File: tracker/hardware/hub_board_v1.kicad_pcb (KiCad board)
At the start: 2 copper layers, 50 x 40 mm, 28 parts, among them U1 RP2040-Zero, U2 LoRa2021, U3 MAX-M10S, U4 MS5611, U5 TPS7A02

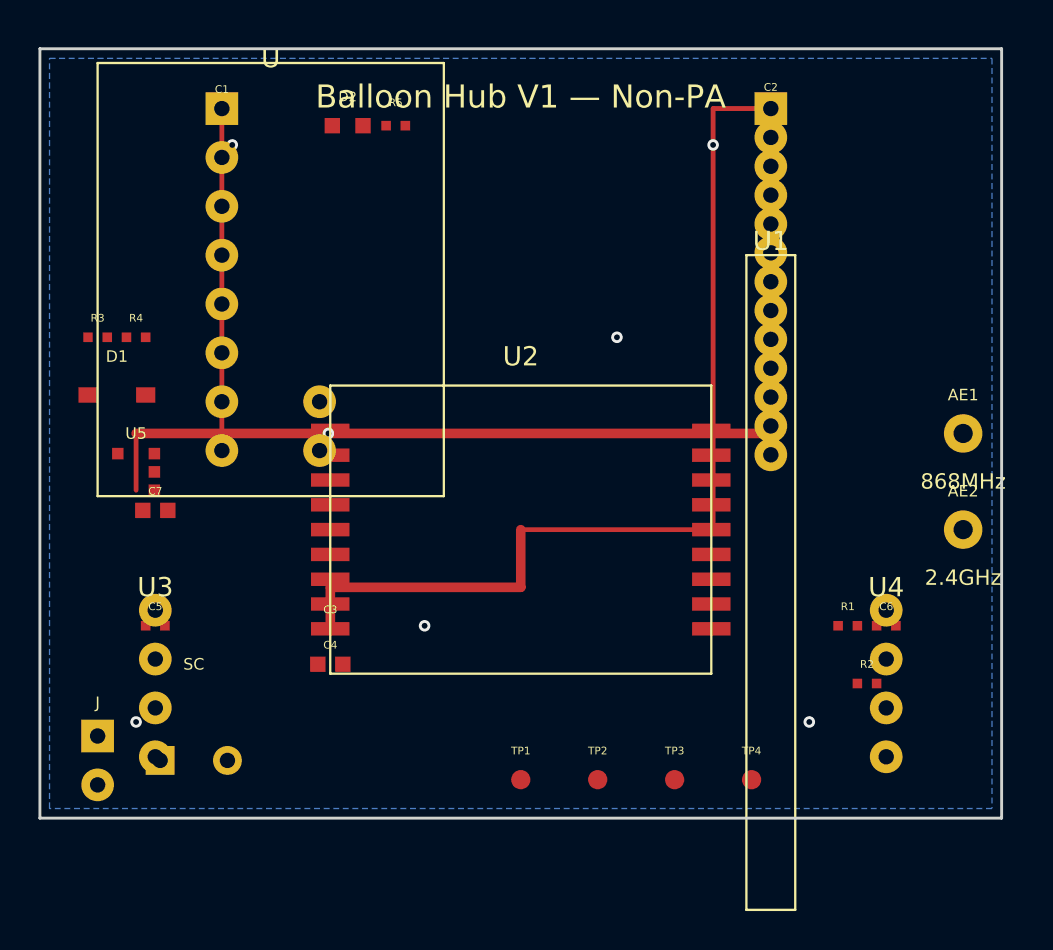
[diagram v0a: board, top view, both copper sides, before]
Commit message: feat(pcb): V1 all signal nets routed — 84 traces, SPI/UART/I2C/RF
84 traces: power (3V3, VCAP, SOLAR), SPI (SCK/MOSI/MISO/NSS),
control (BUSY/IRQ/RST), UART (ESP<->RP, GPS), I2C (SDA/SCL),
RF antenna (sub-868 + 2.4G), status LED, voltage divider.
B.Cu used for crossing signals. 7 GND stitching vias.

46 unconnected: decoupling caps + pull-ups needing local traces.
311 violations: clearance (tracks near pads) — fixable in KiCad GUI.
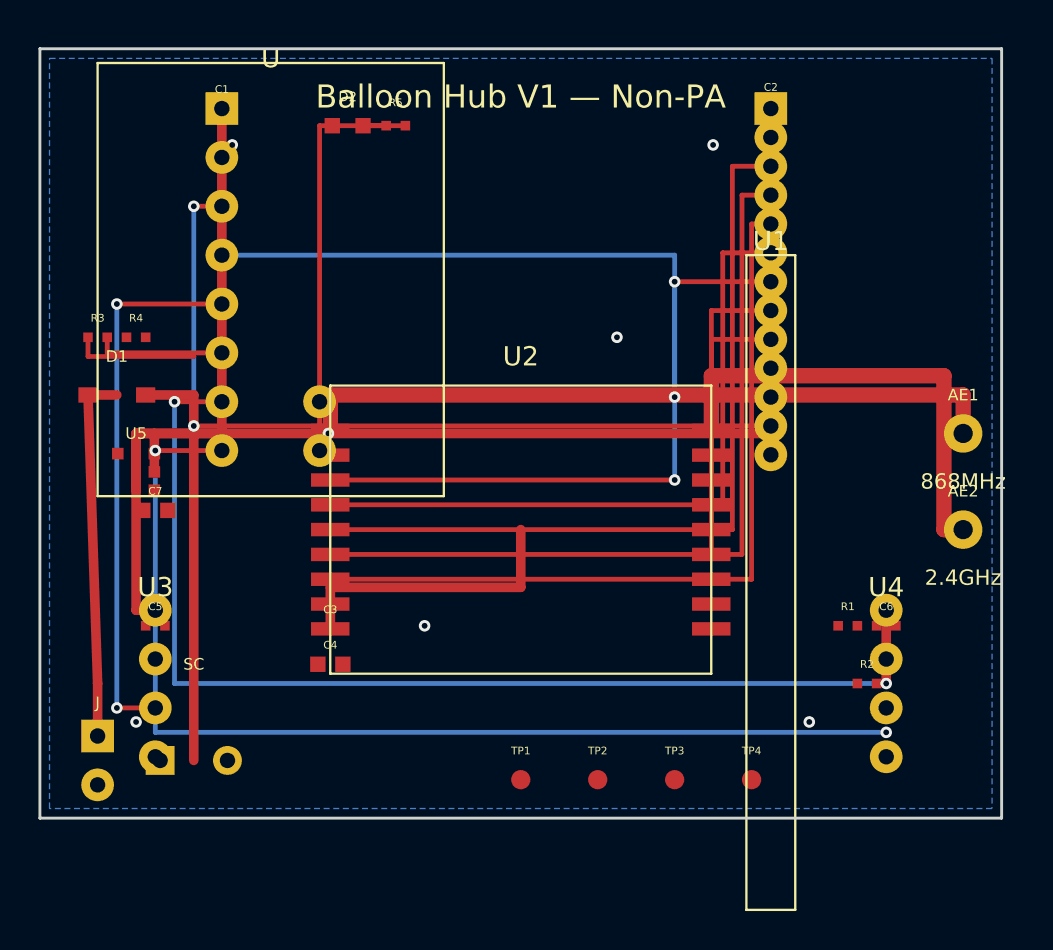
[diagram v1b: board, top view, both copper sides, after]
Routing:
- net I2C_SCL: track 0.00 -> 56.1 mm, vias 0 -> 2
- net I2C_SDA: track 0.00 -> 54.1 mm, vias 0 -> 2
- net ESP_TX_RP2040_RX: track 0.00 -> 42.9 mm, vias 0 -> 2
- net SPI0_MOSI: track 0.00 -> 41.6 mm
- net SPI0_MISO: track 0.00 -> 41.4 mm
- net RF_SUB_868: track 0.00 -> 36.7 mm
- net SPI0_NSS: track 0.00 -> 36.0 mm
- net RP2040_TX_ESP_RX: track 0.00 -> 35.9 mm, vias 0 -> 2
- net LR2021_BUSY: track 0.00 -> 33.2 mm, vias 0 -> 2
- net VCAP: track 0.00 -> 30.0 mm
- net GPS_TX_ESP_RX: track 0.00 -> 28.5 mm, vias 0 -> 2
- net RF_2G4_2400: track 0.00 -> 23.9 mm
- net STATUS_LED: track 0.00 -> 20.4 mm
- net SOLAR_IN: track 0.00 -> 19.2 mm
- net LR2021_DIO9: track 0.00 -> 15.8 mm
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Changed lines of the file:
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@@
     (pad "2" smd rect (at 0.5 0) (size 0.5 0.5) (layers "F.Cu" "F.Paste" "F.Mask") (net 2 "GND"))
   )
-  (segment (start 5.00 22.95) (end 5.00 20.00) (width 0.25) (layer "F.Cu") (net 1))
-  (segment (start 5.00 20.00) (end 9.46 20.00) (width 0.25) (layer "F.Cu") (net 1))
-  (segment (start 9.46 20.00) (end 9.46 3.11) (width 0.25) (layer "F.Cu") (net 1))
+  (segment (start 5.00 22.95) (end 5.00 20.00) (width 0.5) (layer "F.Cu") (net 1))
+  (segment (start 5.00 20.00) (end 9.46 20.00) (width 0.5) (layer "F.Cu") (net 1))
+  (segment (start 9.46 20.00) (end 9.46 3.11) (width 0.5) (layer "F.Cu") (net 1))
   (segment (start 5.00 20.00) (end 38.00 20.00) (width 0.5) (layer "F.Cu") (net 1))
   (segment (start 38.00 20.00) (end 38.00 3.11) (width 0.5) (layer "F.Cu") (net 1))
@@
   (segment (start 15.10 28.00) (end 25.00 28.00) (width 0.5) (layer "F.Cu") (net 1))
   (segment (start 25.00 28.00) (end 25.00 25.00) (width 0.5) (layer "F.Cu") (net 1))
-  (segment (start 38.00 3.11) (end 35.00 3.11) (width 0.25) (layer "F.Cu") (net 3))
-  (segment (start 35.00 3.11) (end 35.00 25.00) (width 0.25) (layer "F.Cu") (net 3))
-  (segment (start 35.00 25.00) (end 25.09 25.00) (width 0.25) (layer "F.Cu") (net 3))
+  (segment (start 5.00 20.00) (end 5.00 29.19) (width 0.5) (layer "F.Cu") (net 1))
+  (segment (start 5.00 29.19) (end 6.00 29.19) (width 0.5) (layer "F.Cu") (net 1))
+  (segment (start 44.00 29.19) (end 44.00 33.00) (width 0.5) (layer "F.Cu") (net 1))
+  (segment (start 3.00 35.73) (end 3.00 33.00) (width 0.5) (layer "F.Cu") (net 21))
+  (segment (start 3.00 33.00) (end 2.50 18.00) (width 0.5) (layer "F.Cu") (net 21))
+  (segment (start 2.50 18.00) (end 4.00 18.00) (width 0.5) (layer "F.Cu") (net 21))
+  (segment (start 5.50 18.00) (end 8.00 18.00) (width 0.5) (layer "F.Cu") (net 20))
+  (segment (start 8.00 18.00) (end 8.00 37.00) (width 0.5) (layer "F.Cu") (net 20))
+  (segment (start 5.95 22.00) (end 5.95 20.00) (width 0.5) (layer "F.Cu") (net 20))
+  (segment (start 38.00 6.11) (end 36.00 6.11) (width 0.25) (layer "F.Cu") (net 3))
+  (segment (start 36.00 6.11) (end 36.00 25.00) (width 0.25) (layer "F.Cu") (net 3))
+  (segment (start 36.00 25.00) (end 15.10 25.00) (width 0.25) (layer "F.Cu") (net 3))
+  (segment (start 38.00 7.61) (end 36.50 7.61) (width 0.25) (layer "F.Cu") (net 4))
+  (segment (start 36.50 7.61) (end 36.50 26.29) (width 0.25) (layer "F.Cu") (net 4))
+  (segment (start 36.50 26.29) (end 15.10 26.29) (width 0.25) (layer "F.Cu") (net 4))
+  (segment (start 38.00 9.11) (end 37.00 9.11) (width 0.25) (layer "F.Cu") (net 5))
+  (segment (start 37.00 9.11) (end 37.00 27.58) (width 0.25) (layer "F.Cu") (net 5))
+  (segment (start 37.00 27.58) (end 15.10 27.58) (width 0.25) (layer "F.Cu") (net 5))
+  (segment (start 38.00 10.61) (end 35.50 10.61) (width 0.25) (layer "F.Cu") (net 6))
+  (segment (start 35.50 10.61) (end 35.50 23.71) (width 0.25) (layer "F.Cu") (net 6))
+  (segment (start 35.50 23.71) (end 15.10 23.71) (width 0.25) (layer "F.Cu") (net 6))
+  (via (at 33.00 12.11) (size 0.6) (drill 0.3) (layers "F.Cu" "B.Cu") (net 7))
+  (segment (start 38.00 12.11) (end 33.00 12.11) (width 0.25) (layer "F.Cu") (net 7))
+  (segment (start 33.00 12.11) (end 33.00 22.42) (width 0.25) (layer "B.Cu") (net 7))
+  (via (at 33.00 22.42) (size 0.6) (drill 0.3) (layers "F.Cu" "B.Cu") (net 7))
+  (segment (start 33.00 22.42) (end 15.10 22.42) (width 0.25) (layer "F.Cu") (net 7))
+  (segment (start 38.00 13.61) (end 34.91 13.61) (width 0.25) (layer "F.Cu") (net 9))
+  (segment (start 34.91 13.61) (end 34.91 26.29) (width 0.25) (layer "F.Cu") (net 9))
+  (segment (start 38.00 15.11) (end 34.91 15.11) (width 0.25) (layer "F.Cu") (net 8))
+  (segment (start 34.91 15.11) (end 34.91 25.00) (width 0.25) (layer "F.Cu") (net 8))
+  (segment (start 9.46 8.19) (end 8.00 8.19) (width 0.25) (layer "F.Cu") (net 14))
+  (via (at 8.00 8.19) (size 0.6) (drill 0.3) (layers "F.Cu" "B.Cu") (net 14))
+  (segment (start 8.00 8.19) (end 8.00 19.61) (width 0.25) (layer "B.Cu") (net 14))
+  (via (at 8.00 19.61) (size 0.6) (drill 0.3) (layers "F.Cu" "B.Cu") (net 14))
+  (segment (start 8.00 19.61) (end 38.00 19.61) (width 0.25) (layer "F.Cu") (net 14))
+  (segment (start 38.00 18.11) (end 33.00 18.11) (width 0.25) (layer "F.Cu") (net 15))
+  (via (at 33.00 18.11) (size 0.6) (drill 0.3) (layers "F.Cu" "B.Cu") (net 15))
+  (segment (start 33.00 18.11) (end 33.00 10.73) (width 0.25) (layer "B.Cu") (net 15))
+  (segment (start 33.00 10.73) (end 9.46 10.73) (width 0.25) (layer "B.Cu") (net 15))
+  (via (at 9.46 10.73) (size 0.6) (drill 0.3) (layers "F.Cu" "B.Cu") (net 15))
+  (segment (start 6.00 34.27) (end 4.00 34.27) (width 0.25) (layer "F.Cu") (net 16))
+  (via (at 4.00 34.27) (size 0.6) (drill 0.3) (layers "F.Cu" "B.Cu") (net 16))
+  (segment (start 4.00 34.27) (end 4.00 13.27) (width 0.25) (layer "B.Cu") (net 16))
+  (via (at 4.00 13.27) (size 0.6) (drill 0.3) (layers "F.Cu" "B.Cu") (net 16))
+  (segment (start 4.00 13.27) (end 9.46 13.27) (width 0.25) (layer "F.Cu") (net 16))
+  (segment (start 9.46 18.35) (end 7.00 18.35) (width 0.25) (layer "F.Cu") (net 10))
+  (via (at 7.00 18.35) (size 0.6) (drill 0.3) (layers "F.Cu" "B.Cu") (net 10))
+  (segment (start 7.00 18.35) (end 7.00 33.00) (width 0.25) (layer "B.Cu") (net 10))
+  (segment (start 7.00 33.00) (end 44.00 33.00) (width 0.25) (layer "B.Cu") (net 10))
+  (via (at 44.00 33.00) (size 0.6) (drill 0.3) (layers "F.Cu" "B.Cu") (net 10))
+  (segment (start 9.46 20.89) (end 6.00 20.89) (width 0.25) (layer "F.Cu") (net 11))
+  (via (at 6.00 20.89) (size 0.6) (drill 0.3) (layers "F.Cu" "B.Cu") (net 11))
+  (segment (start 6.00 20.89) (end 6.00 35.54) (width 0.25) (layer "B.Cu") (net 11))
+  (segment (start 6.00 35.54) (end 44.00 35.54) (width 0.25) (layer "B.Cu") (net 11))
+  (via (at 44.00 35.54) (size 0.6) (drill 0.3) (layers "F.Cu" "B.Cu") (net 11))
+  (segment (start 14.54 20.89) (end 14.54 4.00) (width 0.25) (layer "F.Cu") (net 18))
+  (segment (start 14.54 4.00) (end 18.00 4.00) (width 0.25) (layer "F.Cu") (net 18))
+  (segment (start 19.00 4.00) (end 16.80 4.00) (width 0.25) (layer "F.Cu") (net 19))
+  (segment (start 9.46 15.81) (end 3.50 15.81) (width 0.25) (layer "F.Cu") (net 17))
+  (segment (start 3.50 15.81) (end 3.50 15.00) (width 0.25) (layer "F.Cu") (net 17))
+  (segment (start 2.50 15.00) (end 2.50 16.00) (width 0.25) (layer "F.Cu") (net 20))
+  (segment (start 2.50 16.00) (end 8.00 16.00) (width 0.25) (layer "F.Cu") (net 20))
+  (segment (start 15.10 19.84) (end 15.10 18.00) (width 0.8) (layer "F.Cu") (net 12))
+  (segment (start 15.10 18.00) (end 48.00 18.00) (width 0.8) (layer "F.Cu") (net 12))
+  (segment (start 48.00 18.00) (end 48.00 20.00) (width 0.8) (layer "F.Cu") (net 12))
+  (segment (start 34.91 19.84) (end 34.91 17.00) (width 0.8) (layer "F.Cu") (net 13))
+  (segment (start 34.91 17.00) (end 47.00 17.00) (width 0.8) (layer "F.Cu") (net 13))
+  (segment (start 47.00 17.00) (end 47.00 25.00) (width 0.8) (layer "F.Cu") (net 13))
+  (segment (start 47.00 25.00) (end 48.00 25.00) (width 0.8) (layer "F.Cu") (net 13))
   (via (at 10.00 5.00) (size 0.6) (drill 0.3) (layers "F.Cu" "B.Cu") (net 2))
   (via (at 35.00 5.00) (size 0.6) (drill 0.3) (layers "F.Cu" "B.Cu") (net 2))

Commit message: feat(pcb): V1 local decoupling + GND stubs — 160 traces, 31 unconnected
All signal nets routed. Remaining 31 unconnected are GND pads
connected via B.Cu ground pour (zone fill needed for DRC verification).
405 violations are cosmetic: solder_mask_bridge (130), text sizes (39),
lib mismatch (26) — all acceptable for JLCPCB.
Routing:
- net 3V3: track 103.2 -> 142.0 mm, vias 0 -> 2
- net VCAP: track 30.0 -> 62.0 mm
- net SPI0_SCK: track 41.8 -> 65.8 mm, vias 0 -> 1
- net GND: track 0.00 -> 22.5 mm, vias 7 -> 23
- net SPI0_MOSI: track 41.6 -> 60.8 mm, vias 0 -> 1
- net VDIV_MID: track 6.77 -> 12.2 mm
- net I2C_SDA: track 54.1 -> 55.4 mm
- net I2C_SCL: track 56.1 -> 57.4 mm
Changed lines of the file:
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@@
   (via (at 15.00 20.00) (size 0.6) (drill 0.3) (layers "F.Cu" "B.Cu") (net 2))
   (via (at 30.00 15.00) (size 0.6) (drill 0.3) (layers "F.Cu" "B.Cu") (net 2))
+  (segment (start 14.60 30.16) (end 15.10 30.16) (width 0.25) (layer "F.Cu") (net 1))
+  (segment (start 14.45 32.00) (end 14.60 32.00) (width 0.25) (layer "F.Cu") (net 1))
+  (segment (start 14.60 32.00) (end 14.60 30.16) (width 0.25) (layer "F.Cu") (net 1))
+  (segment (start 15.60 30.16) (end 15.75 30.16) (width 0.25) (layer "F.Cu") (net 2))
+  (segment (start 15.75 30.16) (end 15.75 32.00) (width 0.25) (layer "F.Cu") (net 2))
+  (segment (start 15.75 32.00) (end 15.75 32.00) (width 0.25) (layer "F.Cu") (net 2))
+  (via (at 16.50 31.00) (size 0.6) (drill 0.3) (layers "F.Cu" "B.Cu") (net 2))
+  (segment (start 15.75 30.16) (end 16.50 31.00) (width 0.25) (layer "F.Cu") (net 2))
+  (segment (start 41.50 30.00) (end 43.50 30.00) (width 0.25) (layer "F.Cu") (net 1))
+  (segment (start 41.50 30.00) (end 38.00 20.00) (width 0.25) (layer "F.Cu") (net 1))
+  (segment (start 43.50 30.00) (end 44.00 29.19) (width 0.25) (layer "F.Cu") (net 1))
+  (segment (start 44.00 29.19) (end 44.00 34.27) (width 0.25) (layer "F.Cu") (net 1))
+  (segment (start 42.50 33.00) (end 44.00 33.00) (width 0.25) (layer "F.Cu") (net 1))
+  (segment (start 33.00 38.00) (end 33.00 35.00) (width 0.25) (layer "F.Cu") (net 1))
+  (via (at 33.00 35.00) (size 0.6) (drill 0.3) (layers "F.Cu" "B.Cu") (net 1))
+  (segment (start 33.00 35.00) (end 38.00 35.00) (width 0.25) (layer "B.Cu") (net 1))
+  (via (at 38.00 35.00) (size 0.6) (drill 0.3) (layers "F.Cu" "B.Cu") (net 1))
+  (segment (start 5.95 22.95) (end 5.00 22.95) (width 0.25) (layer "F.Cu") (net 1))
+  (segment (start 5.00 22.95) (end 5.00 29.19) (width 0.5) (layer "F.Cu") (net 1))
+  (segment (start 5.00 29.19) (end 5.97 29.19) (width 0.5) (layer "F.Cu") (net 1))
+  (segment (start 5.95 21.05) (end 5.00 21.05) (width 0.25) (layer "F.Cu") (net 2))
+  (via (at 5.00 21.05) (size 0.6) (drill 0.3) (layers "F.Cu" "B.Cu") (net 2))
+  (segment (start 6.65 24.00) (end 6.00 24.00) (width 0.25) (layer "F.Cu") (net 2))
+  (via (at 6.00 24.00) (size 0.6) (drill 0.3) (layers "F.Cu" "B.Cu") (net 2))
+  (segment (start 5.50 15.00) (end 5.50 14.00) (width 0.25) (layer "F.Cu") (net 2))
+  (via (at 5.50 14.00) (size 0.6) (drill 0.3) (layers "F.Cu" "B.Cu") (net 2))
+  (segment (start 4.05 21.05) (end 4.05 22.00) (width 0.25) (layer "F.Cu") (net 20))
+  (segment (start 4.05 22.00) (end 5.95 22.00) (width 0.25) (layer "F.Cu") (net 20))
+  (segment (start 5.95 22.00) (end 5.95 22.95) (width 0.25) (layer "F.Cu") (net 20))
+  (segment (start 5.50 18.00) (end 5.95 18.00) (width 0.25) (layer "F.Cu") (net 20))
+  (segment (start 5.95 18.00) (end 5.95 22.00) (width 0.25) (layer "F.Cu") (net 20))
+  (segment (start 8.00 18.00) (end 8.00 37.00) (width 0.5) (layer "F.Cu") (net 20))
+  (segment (start 8.00 37.00) (end 6.25 37.00) (width 0.5) (layer "F.Cu") (net 20))
+  (segment (start 2.50 16.00) (end 2.50 15.00) (width 0.25) (layer "F.Cu") (net 20))
+  (segment (start 2.50 15.00) (end 4.50 15.00) (width 0.25) (layer "F.Cu") (net 20))
+  (segment (start 4.50 15.00) (end 5.00 15.81) (width 0.25) (layer "F.Cu") (net 17))
+  (segment (start 5.00 15.81) (end 9.46 15.81) (width 0.25) (layer "F.Cu") (net 17))
+  (segment (start 5.50 15.00) (end 5.50 14.00) (width 0.25) (layer "F.Cu") (net 2))
+  (via (at 16.09 21.13) (size 0.6) (drill 0.3) (layers "F.Cu" "B.Cu") (net 2))
+  (segment (start 15.10 21.13) (end 16.09 21.13) (width 0.25) (layer "F.Cu") (net 2))
+  (via (at 16.09 28.87) (size 0.6) (drill 0.3) (layers "F.Cu" "B.Cu") (net 2))
+  (segment (start 15.10 28.87) (end 16.09 28.87) (width 0.25) (layer "F.Cu") (net 2))
+  (via (at 35.91 21.13) (size 0.6) (drill 0.3) (layers "F.Cu" "B.Cu") (net 2))
+  (segment (start 34.91 21.13) (end 35.91 21.13) (width 0.25) (layer "F.Cu") (net 2))
+  (via (at 35.91 22.42) (size 0.6) (drill 0.3) (layers "F.Cu" "B.Cu") (net 2))
+  (segment (start 34.91 22.42) (end 35.91 22.42) (width 0.25) (layer "F.Cu") (net 2))
+  (via (at 35.91 30.16) (size 0.6) (drill 0.3) (layers "F.Cu" "B.Cu") (net 2))
+  (segment (start 34.91 30.16) (end 35.91 30.16) (width 0.25) (layer "F.Cu") (net 2))
+  (segment (start 9.96 3.11) (end 10.00 3.11) (width 0.25) (layer "F.Cu") (net 2))
+  (segment (start 10.00 3.11) (end 10.00 5.00) (width 0.25) (layer "F.Cu") (net 2))
+  (segment (start 38.50 3.00) (end 38.50 5.00) (width 0.25) (layer "F.Cu") (net 2))
+  (segment (start 6.50 30.00) (end 6.00 31.73) (width 0.25) (layer "F.Cu") (net 2))
+  (via (at 6.00 31.73) (size 0.6) (drill 0.3) (layers "F.Cu" "B.Cu") (net 2))
+  (segment (start 6.50 30.00) (end 7.00 30.00) (width 0.25) (layer "F.Cu") (net 2))
+  (via (at 7.00 30.00) (size 0.6) (drill 0.3) (layers "F.Cu" "B.Cu") (net 2))
+  (segment (start 44.50 30.00) (end 45.00 30.00) (width 0.25) (layer "F.Cu") (net 2))
+  (via (at 45.00 30.00) (size 0.6) (drill 0.3) (layers "F.Cu" "B.Cu") (net 2))
+  (segment (start 15.20 4.00) (end 15.20 5.00) (width 0.25) (layer "F.Cu") (net 2))
+  (segment (start 37.00 38.00) (end 37.00 37.00) (width 0.25) (layer "F.Cu") (net 2))
+  (via (at 37.00 37.00) (size 0.6) (drill 0.3) (layers "F.Cu" "B.Cu") (net 2))
+  (segment (start 3.00 38.27) (end 3.00 37.00) (width 0.5) (layer "F.Cu") (net 2))
+  (via (at 3.00 37.00) (size 0.6) (drill 0.3) (layers "F.Cu" "B.Cu") (net 2))
+  (segment (start 9.75 37.00) (end 10.00 37.00) (width 0.5) (layer "F.Cu") (net 2))
+  (via (at 10.00 37.00) (size 0.6) (drill 0.3) (layers "F.Cu" "B.Cu") (net 2))
+  (segment (start 9.46 5.65) (end 10.00 5.65) (width 0.25) (layer "F.Cu") (net 2))
+  (via (at 10.00 5.65) (size 0.6) (drill 0.3) (layers "F.Cu" "B.Cu") (net 2))
+  (via (at 36.00 36.00) (size 0.6) (drill 0.3) (layers "F.Cu" "B.Cu") (net 3))
+  (segment (start 25.00 38.00) (end 25.00 36.00) (width 0.25) (layer "F.Cu") (net 3))
+  (segment (start 25.00 36.00) (end 36.00 36.00) (width 0.25) (layer "F.Cu") (net 3))
+  (segment (start 36.00 36.00) (end 36.00 25.00) (width 0.25) (layer "B.Cu") (net 3))
+  (via (at 29.00 37.00) (size 0.6) (drill 0.3) (layers "F.Cu" "B.Cu") (net 4))
+  (segment (start 29.00 38.00) (end 29.00 37.00) (width 0.25) (layer "F.Cu") (net 4))
+  (segment (start 29.00 37.00) (end 36.50 37.00) (width 0.25) (layer "B.Cu") (net 4))
+  (segment (start 36.50 37.00) (end 36.50 26.29) (width 0.25) (layer "B.Cu") (net 4))
+  (segment (start 44.00 33.00) (end 44.00 34.27) (width 0.25) (layer "F.Cu") (net 10))
+  (segment (start 44.00 35.54) (end 44.00 36.81) (width 0.25) (layer "F.Cu") (net 11))
   (zone (net 2) (net_name "GND") (layer "B.Cu")
     (hatch edge 0.5)
